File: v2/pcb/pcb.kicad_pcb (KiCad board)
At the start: 2 copper layers, 14 parts, among them J1 LED STRIP, J2 RV3028, SW1 TIME, SW2 BRIGHTNESS, SW3 MODE, SW4 DAYLIGHT SAVING, U1 PRO MICRO

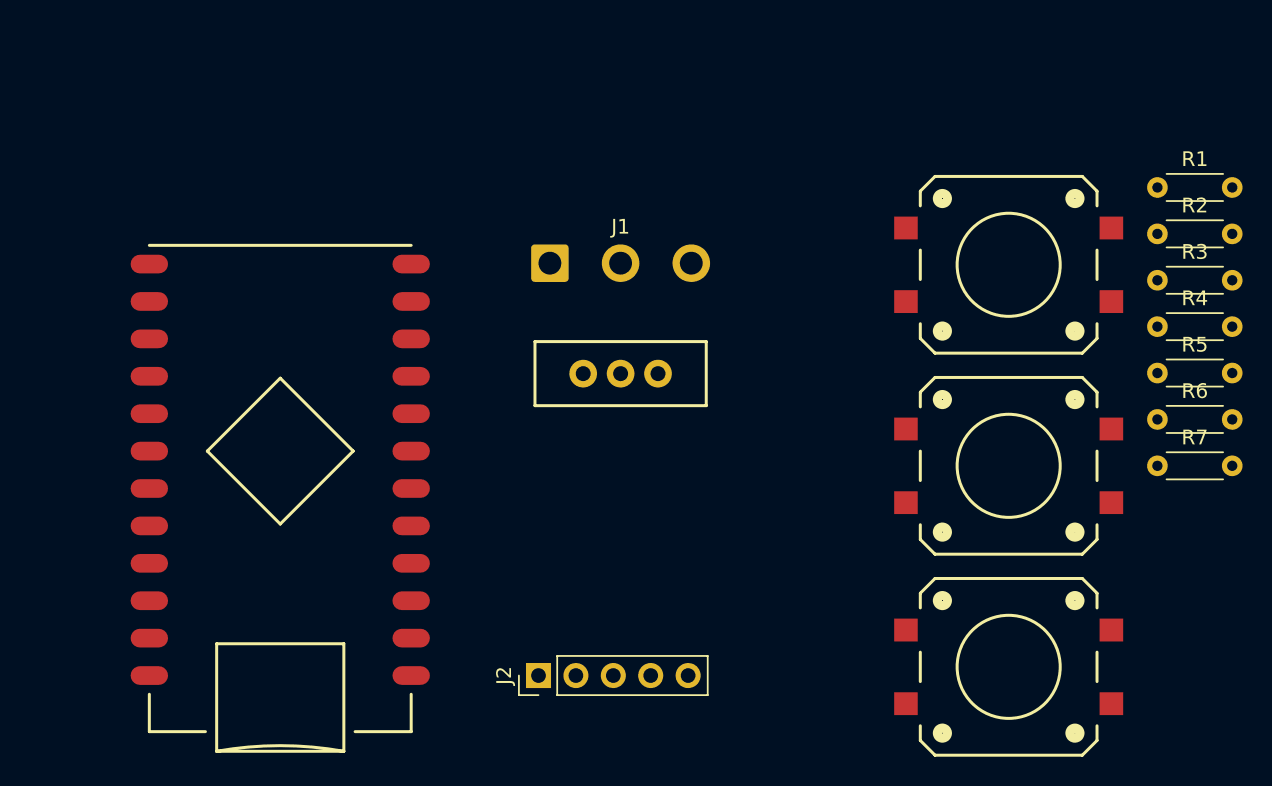
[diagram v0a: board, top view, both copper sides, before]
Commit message: [PCB] New PCB mostly complete
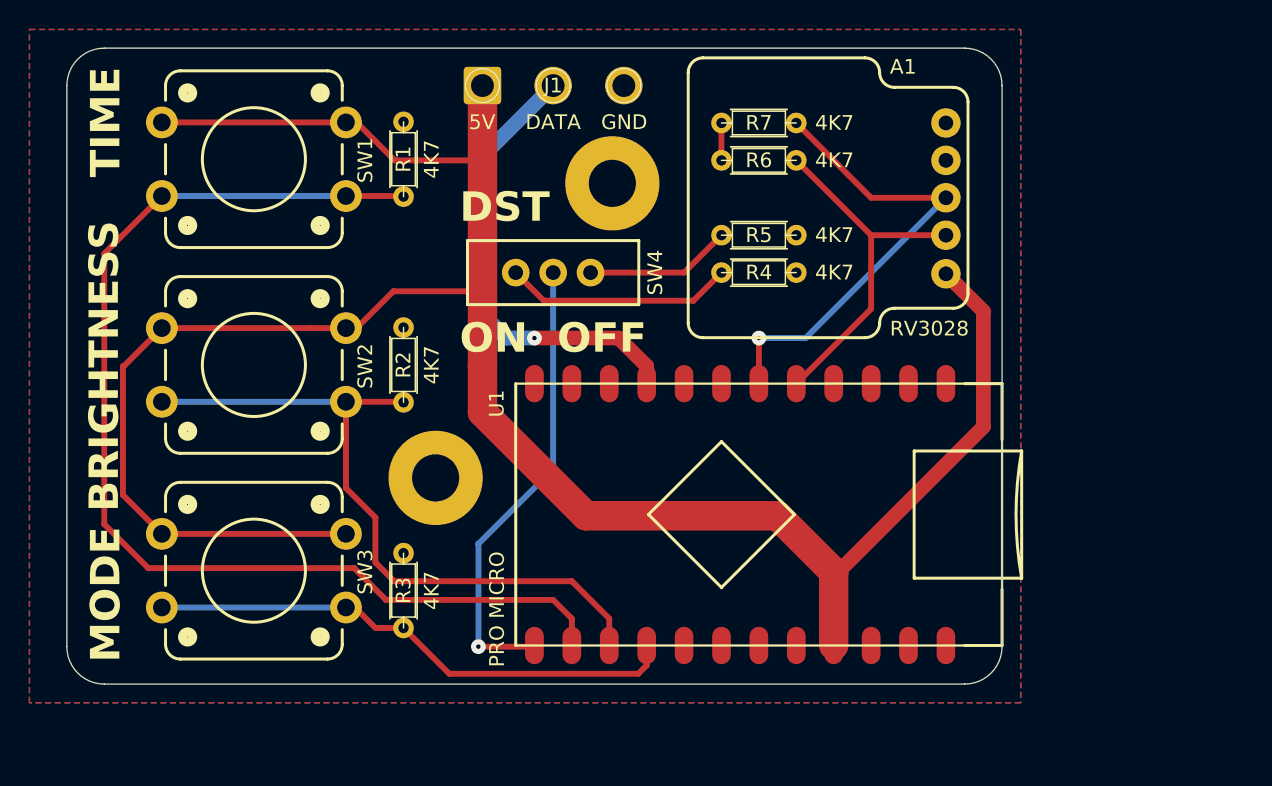
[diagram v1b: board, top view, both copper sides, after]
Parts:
- removed J2: RV3028, Connector_PinHeader_2.54mm:PinHeader_1x05_P2.54mm_Vertical
- added A1: RV3028, Pimoroni_RV3028:Pimoroni_RV3028_Breakout, F.Cu at (86.6, 45.1)
- added H1: MountingHole, MountingHole:MountingHole_3.2mm_M3_Pad, F.Cu at (50.4, 54.6)
- added H2: MountingHole, MountingHole:MountingHole_3.2mm_M3_Pad, F.Cu at (62.4, 34.6)
- SW1, SW2, SW3: footprint SparkFun-Switch:Push_SMD_12x12mm -> SparkFun-Switch:Push_PTH_12x12mm
- SW4: value DAYLIGHT SAVING -> DST
- moved R3 56.4 mm to (48.3, 64.8), turned to 90 degrees
- moved R2 52.5 mm to (48.3, 49.5), turned to 90 degrees
- moved SW1 51.7 mm to (38.1, 32.9)
- moved SW2 51.7 mm to (38.1, 46.9)
- moved SW3 51.7 mm to (38.1, 60.9)
- moved R1 51.2 mm to (48.3, 35.5), turned to 90 degrees
- moved R6 34.4 mm to (69.8, 33.0)
- moved R7 33.8 mm to (74.9, 30.5), turned to 180 degrees
- moved U1 32.5 mm to (72.4, 57.1), turned to -90 degrees
- moved R4 29.8 mm to (69.8, 40.6)
- moved R5 26.2 mm to (74.9, 38.1), turned to 180 degrees
- moved J1 12.9 mm to (53.6, 27.9)
- moved SW4 8.25 mm to (58.4, 40.6)
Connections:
- R1 pad 1: Net-(R1-Pad1) -> SW1
- R2 pad 1: Net-(R2-Pad1) -> SW2
- R3 pad 1: Net-(R3-Pad1) -> SW3
- R7 pad 1: VCC -> SCL
- R7 pad 2: SCL -> VCC
- SW1 pad 2: Net-(R1-Pad1) -> SW1
- SW2 pad 2: Net-(R2-Pad1) -> SW2
- SW3 pad 2: Net-(R3-Pad1) -> SW3
- SW4 pad 2: unconnected-(SW4-B-Pad2) -> SW4
- U1 pad 10: unconnected-(U1-D7-Pad10) -> INT
- U1 pad 13: unconnected-(U1-D10/A10-Pad13) -> SW4
- U1 pad 14: unconnected-(U1-D16-Pad14) -> SW1
- U1 pad 15: unconnected-(U1-D14-Pad15) -> SW2
- U1 pad 16: unconnected-(U1-D15-Pad16) -> SW3
- U1 pad 5: unconnected-(U1-D2-Pad5) -> SDA
- U1 pad 6: unconnected-(U1-D3-Pad6) -> SCL
- U1 pad 8: LEDDATA -> unconnected-(U1-D5-Pad8)
- U1 pad 9: unconnected-(U1-D6/A7-Pad9) -> LEDDATA
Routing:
- net VCC: track 0.00 -> 160.3 mm
- net SW1: track 0.00 -> 75.8 mm
- net SW2: track 0.00 -> 46.7 mm
- net SW3: track 0.00 -> 35.7 mm
- net SCL: track 0.00 -> 32.0 mm, vias 0 -> 1
- net LEDDATA: track 0.00 -> 31.5 mm, vias 0 -> 1
- net SW4: track 0.00 -> 31.3 mm, vias 0 -> 1
- net SDA: track 0.00 -> 24.4 mm
- net Net-(SW4-A): track 0.00 -> 15.5 mm
- net Net-(SW4-C): track 0.00 -> 9.94 mm
- added copper zone on B.Cu, net GND
- added copper zone on F.Cu, net GND
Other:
- board outline added: 63.5 x 43.2 mm
- board text added: "5V"
- board text added: "DATA"
- board text added: "GND"
- board text added: "OFF"
- board text added: "ON"

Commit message: [PCB] Final design and gerber
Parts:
- moved H1 0.54 mm to (49.9, 54.6)
- moved H2 0.54 mm to (61.9, 34.6)
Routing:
- net INT: track 0.00 -> 32.4 mm, vias 0 -> 1
- net VCC: track 160.3 -> 187.8 mm
- net LEDDATA: track 31.5 -> 34.7 mm
- net SW4: track 31.3 -> 29.6 mm
- net GND: vias 0 -> 1
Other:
- board text added: "WORD CLOCK V2 BY JAROD LAM"
